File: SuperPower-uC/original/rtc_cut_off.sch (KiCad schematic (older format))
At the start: 6 parts, among them J4 Conn_01x02_Male, U3 RV-3028-C7

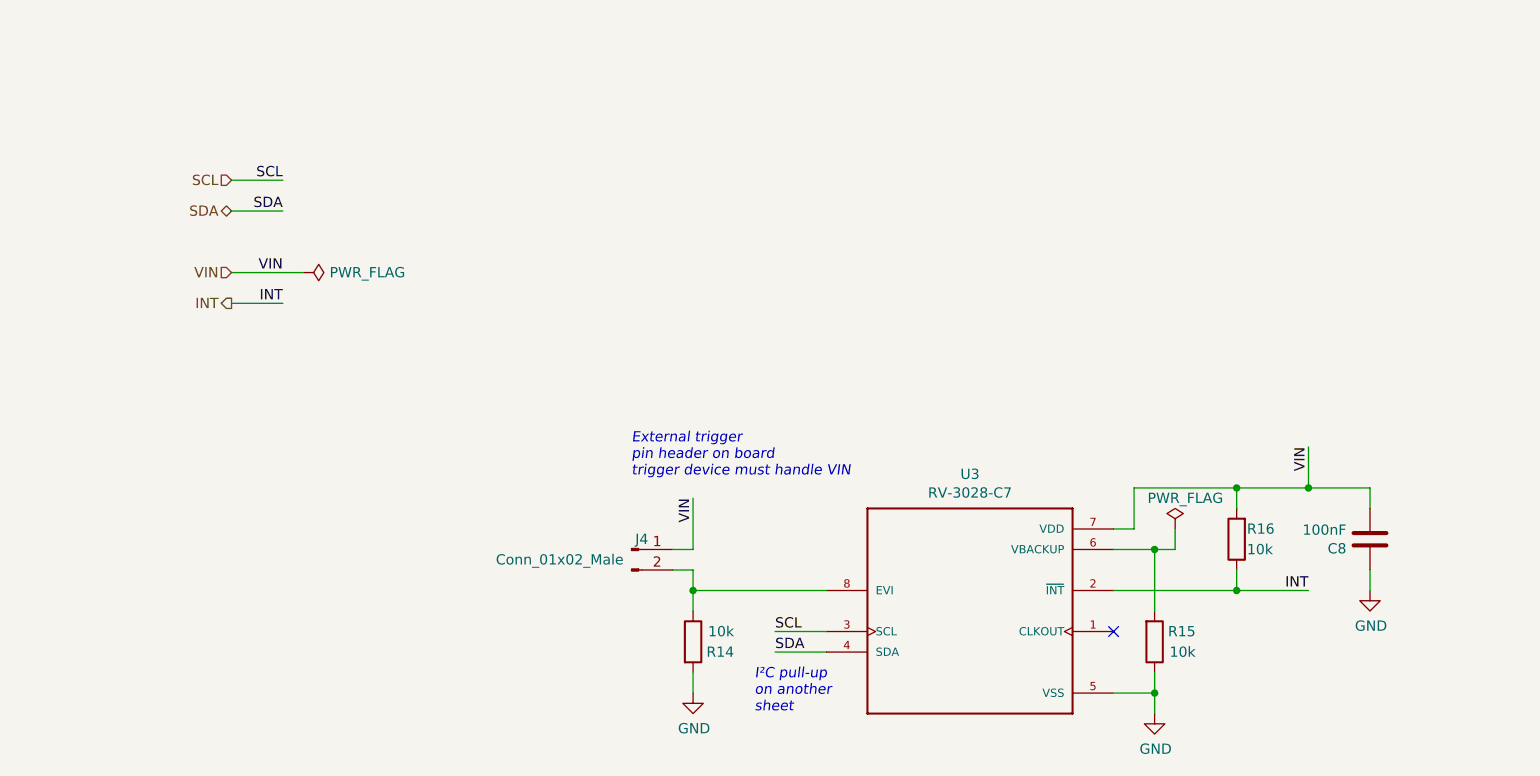
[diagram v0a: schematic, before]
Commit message: Complete rework of regulator design
Removed the old regulator in favor of the TPS63070 and TPS709.
Rewired the RTC and I2C pullups to the TPS709.
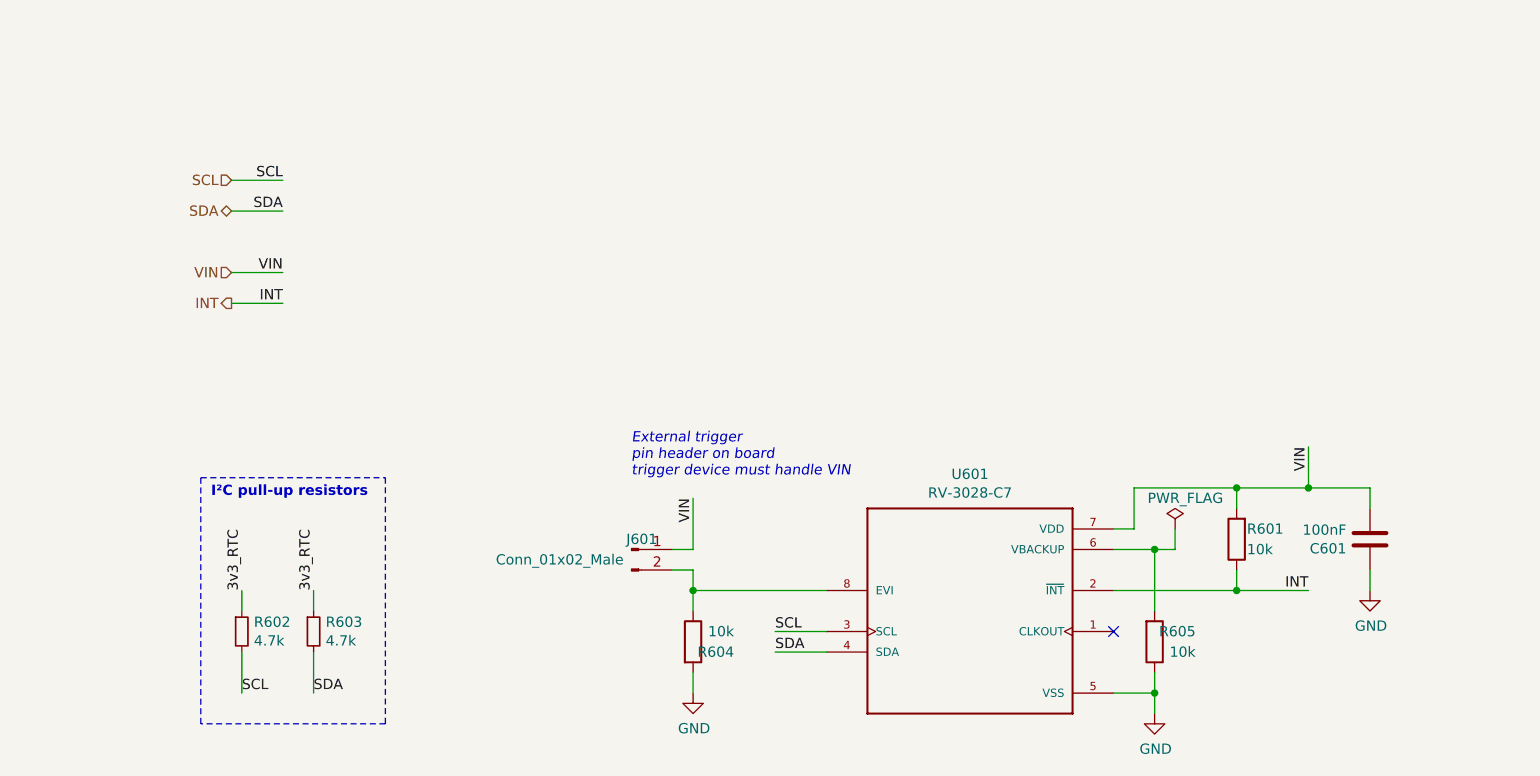
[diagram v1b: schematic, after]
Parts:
- added R602, R603: 4.7k, Resistor_SMD:R_0603_1608Metric_Pad0.98x0.95mm_HandSolder, symbol Device:R_Small
- renumbered C8 to C601, J4 to J601, R16 to R601, R14 to R604, R15 to R605, U3 to U601
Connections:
- net SCL: now also R602.2
- net SDA: now also R603.2
- new net 3v3_RTC: R602.1, R603.1
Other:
- note added: "I²C pull-up resistors"
- note removed: "I²C pull-up\non another\nsheet"
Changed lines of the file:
@@
 $Descr A4 11693 8268
 encoding utf-8
-Sheet 4 7
+Sheet 6 7
 Title "SuperPower-uC"
 Date "2020-09-20"
@@
 NoConn ~ 5900 3550
 $Comp
-L Device:R R15
+L Device:R R605
 U 1 1 5F716104
 P 6100 3600
-F 0 "R15" H 6300 3550 50  0000 R CNN
+F 0 "R605" H 6300 3550 50  0000 R CNN
 F 1 "10k" H 6300 3650 50  0000 R CNN
 F 2 "Resistor_SMD:R_0603_1608Metric_Pad1.05x0.95mm_HandSolder" V 6030 3600 50  0001 C CNN
@@
 $EndComp
 $Comp
-L power:GND #PWR025
+L power:GND #PWR0603
 U 1 1 5F71610D
 P 6100 3950
-F 0 "#PWR025" H 6100 3700 50  0001 C CNN
+F 0 "#PWR0603" H 6100 3700 50  0001 C CNN
 F 1 "GND" H 6105 3777 50  0000 C CNN
 F 2 "" H 6100 3950 50  0001 C CNN
@@
 $EndComp
 $Comp
-L Device:R R16
+L Device:R R601
 U 1 1 5F716136
 P 6500 3100
-F 0 "R16" H 6450 3050 50  0000 R CNN
+F 0 "R601" H 6450 3050 50  0000 R CNN
 F 1 "10k" H 6450 3150 50  0000 R CNN
 F 2 "Resistor_SMD:R_0603_1608Metric_Pad1.05x0.95mm_HandSolder" V 6430 3100 50  0001 C CNN
@@
 	4250 3650 4500 3650
 $Comp
-L RV-3028-C7:RV-3028-C7 U3
+L RV-3028-C7:RV-3028-C7 U601
 U 1 1 5F7160EF
 P 5200 3450
-F 0 "U3" H 5200 4117 50  0000 C CNN
+F 0 "U601" H 5200 4117 50  0000 C CNN
 F 1 "RV-3028-C7" H 5200 4026 50  0000 C CNN
 F 2 "RV-3028-C7:IC_RV-3028-C7" H 5200 3450 50  0001 L BNN
@@
 Text Label 1850 1950 2    50   ~ 0
 INT
-Text Notes 4150 3950 0    50   Italic 0
-I²C pull-up\non another\nsheet
 Text Notes 3550 2800 0    50   Italic 0
 External trigger\npin header on board\ntrigger device must handle VIN
@@
 Wire Wire Line
 	1600 1500 1850 1500
-$Comp
-L power:PWR_FLAG #FLG06
-U 1 1 5F765992
-P 1950 1800
-F 0 "#FLG06" H 1950 1875 50  0001 C CNN
-F 1 "PWR_FLAG" V 1950 1928 50  0000 L CNN
-F 2 "" H 1950 1800 50  0001 C CNN
-F 3 "~" H 1950 1800 50  0001 C CNN
-	1    1950 1800
-	0    1    1    0
-$EndComp
-Wire Wire Line
-	1600 1800 1950 1800
+Wire Wire Line
+	1600 1800 1850 1800
 Wire Wire Line
 	4500 3550 4250 3550
 $Comp
-L Device:C C8
+L Device:C C601
 U 1 1 5F716113
 P 7150 3100
-F 0 "C8" H 7265 3146 50  0000 L CNN
+F 0 "C601" H 7265 3146 50  0000 L CNN
 F 1 "100nF" H 7265 3055 50  0000 L CNN
 F 2 "Capacitor_SMD:C_0603_1608Metric_Pad1.05x0.95mm_HandSolder" H 7188 2950 50  0001 C CNN
@@
 INT
 $Comp
-L power:PWR_FLAG #FLG07
+L power:PWR_FLAG #FLG0601
 U 1 1 5FABB3BB
 P 6200 3050
-F 0 "#FLG07" H 6200 3125 50  0001 C CNN
+F 0 "#FLG0601" H 6200 3125 50  0001 C CNN
 F 1 "PWR_FLAG" H 6250 3200 50  0000 C CNN
 F 2 "" H 6200 3050 50  0001 C CNN
@@
 	3850 3750 3850 3850
 $Comp
-L Connector:Conn_01x02_Male J4
+L Connector:Conn_01x02_Male J601
 U 1 1 5F78D93A
 P 3550 3150
-F 0 "J4" H 3600 3200 50  0000 C CNN
+F 0 "J601" H 3600 3200 50  0000 C CNN
 F 1 "Conn_01x02_Male" H 3200 3100 50  0000 C CNN
 F 2 "" H 3550 3150 50  0001 C CNN
@@
 VIN
 $Comp
-L Device:R R14
+L Device:R R604
 U 1 1 5F716154
 P 3850 3600
-F 0 "R14" H 4050 3550 50  0000 R CNN
+F 0 "R604" H 4050 3550 50  0000 R CNN
 F 1 "10k" H 4050 3650 50  0000 R CNN
 F 2 "Resistor_SMD:R_0603_1608Metric_Pad1.05x0.95mm_HandSolder" V 3780 3600 50  0001 C CNN
@@
 $EndComp
 $Comp
-L power:GND #PWR024
+L power:GND #PWR0602
 U 1 1 5F716148
 P 3850 3850
-F 0 "#PWR024" H 3850 3600 50  0001 C CNN
+F 0 "#PWR0602" H 3850 3600 50  0001 C CNN
 F 1 "GND" H 3855 3677 50  0000 C CNN
 F 2 "" H 3850 3850 50  0001 C CNN
@@
 Connection ~ 6100 3150
 $Comp
-L power:GND #PWR026
+L power:GND #PWR0601
 U 1 1 5FBD2731
 P 7150 3350
-F 0 "#PWR026" H 7150 3100 50  0001 C CNN
+F 0 "#PWR0601" H 7150 3100 50  0001 C CNN
 F 1 "GND" H 7155 3177 50  0000 C CNN
 F 2 "" H 7150 3350 50  0001 C CNN
@@
 Wire Wire Line
 	6850 2650 6850 2850
+$Comp
+L Device:R_Small R?
+U 1 1 5FB76F56
+P 2000 3550
+AR Path="/5F63A193/5FB76F56" Ref="R?"  Part="1"
+AR Path="/5F63A00B/5FB76F56" Ref="R603"  Part="1"
+F 0 "R603" H 2059 3596 50  0000 L CNN
+F 1 "4.7k" H 2059 3505 50  0000 L CNN
+F 2 "Resistor_SMD:R_0603_1608Metric_Pad0.98x0.95mm_HandSolder" H 2000 3550 50  0001 C CNN
+F 3 "~" H 2000 3550 50  0001 C CNN
+	1    2000 3550
+	1    0    0    -1
+$EndComp
+$Comp
+L Device:R_Small R?
+U 1 1 5FB76F5C
+P 1650 3550
+AR Path="/5F63A193/5FB76F5C" Ref="R?"  Part="1"
+AR Path="/5F63A00B/5FB76F5C" Ref="R602"  Part="1"
+F 0 "R602" H 1709 3596 50  0000 L CNN
+F 1 "4.7k" H 1709 3505 50  0000 L CNN
+F 2 "Resistor_SMD:R_0603_1608Metric_Pad0.98x0.95mm_HandSolder" H 1650 3550 50  0001 C CNN
+F 3 "~" H 1650 3550 50  0001 C CNN
+	1    1650 3550
+	1    0    0    -1
+$EndComp
+Wire Wire Line
+	1650 3350 1650 3450
+Wire Wire Line
+	2000 3350 2000 3450
+Wire Wire Line
+	2000 3650 2000 3850
+Wire Wire Line
+	1650 3650 1650 3850
+Text Notes 1500 2900 0    50   ~ 10
+I²C pull-up resistors
+Wire Notes Line
+	1450 2800 2350 2800
+Wire Notes Line
+	1450 4000 1450 2800
+Wire Notes Line
+	2350 4000 1450 4000
+Wire Notes Line
+	2350 2800 2350 4000
+Text Label 1650 3350 1    50   ~ 0
+3v3_RTC
+Text Label 2000 3350 1    50   ~ 0
+3v3_RTC
+Text Label 2000 3850 0    50   ~ 0
+SDA
+Text Label 1650 3850 0    50   ~ 0
+SCL
 $EndSCHEMATC

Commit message: Changed 10k pulldowns to 100k. Cosmetics.
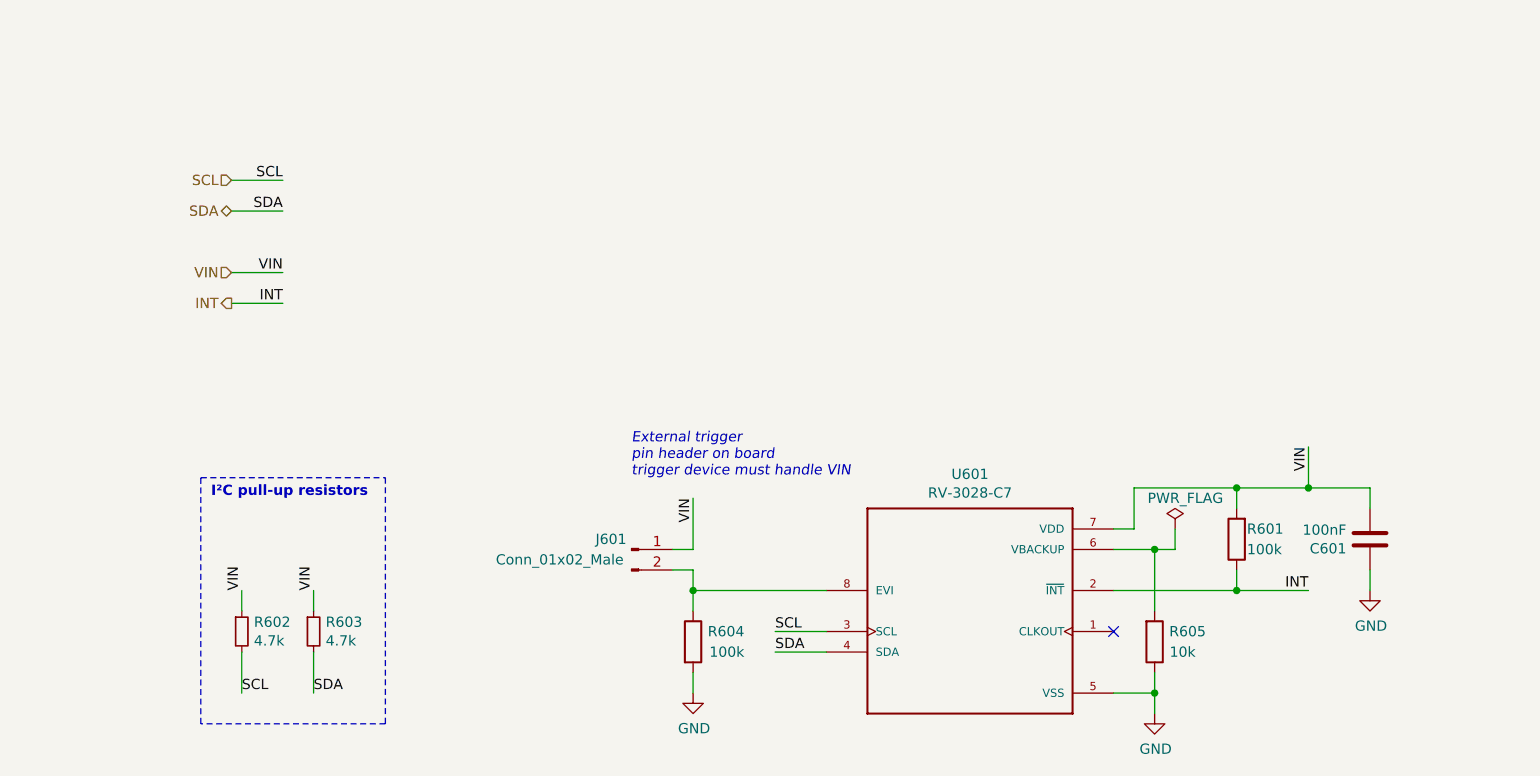
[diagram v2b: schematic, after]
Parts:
- R601, R604: value 10k -> 100k
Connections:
- net 3v3_RTC is gone; now on net VIN: R602.1, R603.1
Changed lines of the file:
@@
 U 1 1 5F716104
 P 6100 3600
-F 0 "R605" H 6300 3550 50  0000 R CNN
+F 0 "R605" H 6350 3550 50  0000 R CNN
 F 1 "10k" H 6300 3650 50  0000 R CNN
 F 2 "Resistor_SMD:R_0603_1608Metric_Pad1.05x0.95mm_HandSolder" V 6030 3600 50  0001 C CNN
@@
 P 6500 3100
 F 0 "R601" H 6450 3050 50  0000 R CNN
-F 1 "10k" H 6450 3150 50  0000 R CNN
+F 1 "100k" H 6450 3150 50  0000 R CNN
 F 2 "Resistor_SMD:R_0603_1608Metric_Pad1.05x0.95mm_HandSolder" V 6430 3100 50  0001 C CNN
 F 3 "~" H 6500 3100 50  0001 C CNN
@@
 U 1 1 5F78D93A
 P 3550 3150
-F 0 "J601" H 3600 3200 50  0000 C CNN
+F 0 "J601" H 3450 3200 50  0000 C CNN
 F 1 "Conn_01x02_Male" H 3200 3100 50  0000 C CNN
 F 2 "" H 3550 3150 50  0001 C CNN
@@
 U 1 1 5F716154
 P 3850 3600
-F 0 "R604" H 4050 3550 50  0000 R CNN
-F 1 "10k" H 4050 3650 50  0000 R CNN
+F 0 "R604" H 4100 3650 50  0000 R CNN
+F 1 "100k" H 4100 3550 50  0000 R CNN
 F 2 "Resistor_SMD:R_0603_1608Metric_Pad1.05x0.95mm_HandSolder" V 3780 3600 50  0001 C CNN
 F 3 "~" H 3850 3600 50  0001 C CNN
@@
 	2350 2800 2350 4000
 Text Label 1650 3350 1    50   ~ 0
-3v3_RTC
+VIN
 Text Label 2000 3350 1    50   ~ 0
-3v3_RTC
+VIN
 Text Label 2000 3850 0    50   ~ 0
 SDA

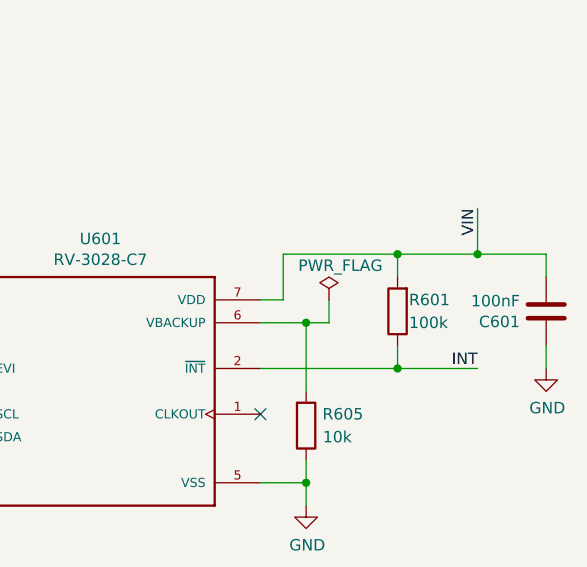
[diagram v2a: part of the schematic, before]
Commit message: Apply first batch of changes fro review ticket
https://github.com/Informaticore/SuperPower/issues/58
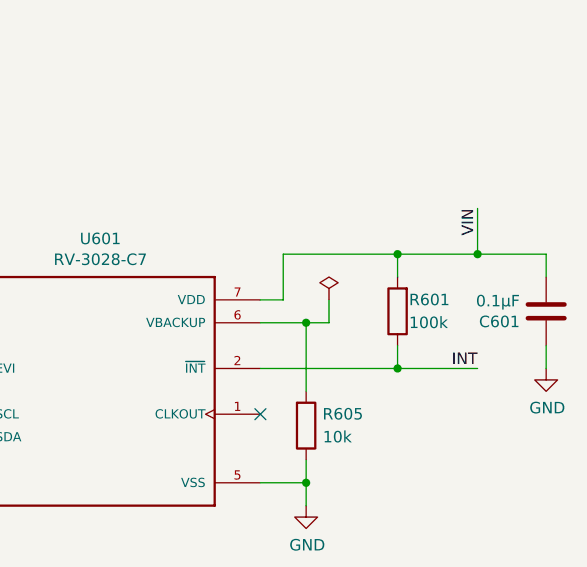
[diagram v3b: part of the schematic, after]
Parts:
- C601: value 100nF -> 0.1µF; footprint Capacitor_SMD:C_0603_1608Metric_Pad1.05x0.95mm_HandSolder -> Capacitors_SMD:C_0603
- R601, R604, R605: footprint Resistor_SMD:R_0603_1608Metric_Pad1.05x0.95mm_HandSolder -> Resistors_SMD:R_0603
- R602, R603: footprint Resistor_SMD:R_0603_1608Metric_Pad0.98x0.95mm_HandSolder -> Resistors_SMD:R_0603
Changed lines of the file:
@@
 F 0 "R605" H 6350 3550 50  0000 R CNN
 F 1 "10k" H 6300 3650 50  0000 R CNN
-F 2 "Resistor_SMD:R_0603_1608Metric_Pad1.05x0.95mm_HandSolder" V 6030 3600 50  0001 C CNN
+F 2 "Resistors_SMD:R_0603" V 6030 3600 50  0001 C CNN
 F 3 "~" H 6100 3600 50  0001 C CNN
 	1    6100 3600
@@
 F 0 "R601" H 6450 3050 50  0000 R CNN
 F 1 "100k" H 6450 3150 50  0000 R CNN
-F 2 "Resistor_SMD:R_0603_1608Metric_Pad1.05x0.95mm_HandSolder" V 6430 3100 50  0001 C CNN
+F 2 "Resistors_SMD:R_0603" V 6430 3100 50  0001 C CNN
 F 3 "~" H 6500 3100 50  0001 C CNN
 	1    6500 3100
@@
 P 7150 3100
 F 0 "C601" H 7265 3146 50  0000 L CNN
-F 1 "100nF" H 7265 3055 50  0000 L CNN
-F 2 "Capacitor_SMD:C_0603_1608Metric_Pad1.05x0.95mm_HandSolder" H 7188 2950 50  0001 C CNN
+F 1 "0.1µF" H 7265 3055 50  0000 L CNN
+F 2 "Capacitors_SMD:C_0603" H 7188 2950 50  0001 C CNN
 F 3 "~" H 7150 3100 50  0001 C CNN
 	1    7150 3100
@@
 P 6200 3050
 F 0 "#FLG0601" H 6200 3125 50  0001 C CNN
-F 1 "PWR_FLAG" H 6250 3200 50  0000 C CNN
+F 1 "PWR_FLAG" H 6250 3200 50  0001 C CNN
 F 2 "" H 6200 3050 50  0001 C CNN
 F 3 "~" H 6200 3050 50  0001 C CNN
@@
 F 0 "R604" H 4100 3650 50  0000 R CNN
 F 1 "100k" H 4100 3550 50  0000 R CNN
-F 2 "Resistor_SMD:R_0603_1608Metric_Pad1.05x0.95mm_HandSolder" V 3780 3600 50  0001 C CNN
+F 2 "Resistors_SMD:R_0603" V 3780 3600 50  0001 C CNN
 F 3 "~" H 3850 3600 50  0001 C CNN
 	1    3850 3600
@@
 F 0 "R603" H 2059 3596 50  0000 L CNN
 F 1 "4.7k" H 2059 3505 50  0000 L CNN
-F 2 "Resistor_SMD:R_0603_1608Metric_Pad0.98x0.95mm_HandSolder" H 2000 3550 50  0001 C CNN
+F 2 "Resistors_SMD:R_0603" H 2000 3550 50  0001 C CNN
 F 3 "~" H 2000 3550 50  0001 C CNN
 	1    2000 3550
@@
 F 0 "R602" H 1709 3596 50  0000 L CNN
 F 1 "4.7k" H 1709 3505 50  0000 L CNN
-F 2 "Resistor_SMD:R_0603_1608Metric_Pad0.98x0.95mm_HandSolder" H 1650 3550 50  0001 C CNN
+F 2 "Resistors_SMD:R_0603" H 1650 3550 50  0001 C CNN
 F 3 "~" H 1650 3550 50  0001 C CNN
 	1    1650 3550

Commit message: Applied more changes from review
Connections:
- net VIN renamed 3v3_RTC
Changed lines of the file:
@@
 Text HLabel 1600 1500 0    50   BiDi ~ 0
 SDA
-Text HLabel 1600 1800 0    50   Input ~ 0
-VIN
 Text HLabel 1600 1950 0    50   Output ~ 0
 INT
@@
 Text Label 1850 1500 2    50   ~ 0
 SDA
-Text Label 1850 1800 2    50   ~ 0
-VIN
 Text Label 1850 1950 2    50   ~ 0
 INT
-Text Notes 3550 2800 0    50   Italic 0
-External trigger\npin header on board\ntrigger device must handle VIN
 Wire Wire Line
 	1600 1950 1850 1950
@@
 Wire Wire Line
 	1600 1500 1850 1500
-Wire Wire Line
-	1600 1800 1850 1800
 Wire Wire Line
 	4500 3550 4250 3550
@@
 	1    0    0    -1
 $EndComp
-Wire Wire Line
-	3850 2900 3850 3150
-Text Label 3850 2900 3    50   ~ 0
-VIN
 $Comp
 L Device:R R604
@@
 Wire Wire Line
 	6500 3350 6850 3350
-Text Label 6850 2650 3    50   ~ 0
-VIN
 Wire Wire Line
 	6850 2850 7150 2850
@@
 	6500 2850 6850 2850
 Connection ~ 6850 2850
-Wire Wire Line
-	6850 2650 6850 2850
 $Comp
 L Device:R_Small R?
@@
 $EndComp
 Wire Wire Line
-	1650 3350 1650 3450
-Wire Wire Line
-	2000 3350 2000 3450
-Wire Wire Line
 	2000 3650 2000 3850
 Wire Wire Line
@@
 Wire Notes Line
 	2350 2800 2350 4000
-Text Label 1650 3350 1    50   ~ 0
-VIN
-Text Label 2000 3350 1    50   ~ 0
-VIN
 Text Label 2000 3850 0    50   ~ 0
 SDA
 Text Label 1650 3850 0    50   ~ 0
 SCL
+Text HLabel 1600 1800 0    50   Input ~ 0
+3v3_RTC
+Text Label 6850 2650 3    50   ~ 0
+VIN
+Wire Wire Line
+	6850 2650 6850 2850
+Wire Wire Line
+	3850 2900 3850 3150
+Text Label 3850 2900 3    50   ~ 0
+VIN
+Text Notes 3550 2800 0    50   Italic 0
+External trigger\npin header on board\ntrigger device must handle VIN
+Text Label 2000 3200 3    50   ~ 0
+VIN
+Text Label 1650 3200 3    50   ~ 0
+VIN
+Wire Wire Line
+	1600 1800 1850 1800
+Text Label 1850 1800 2    50   ~ 0
+VIN
+Wire Wire Line
+	2000 3200 2000 3450
+Wire Wire Line
+	1650 3200 1650 3450
 $EndSCHEMATC

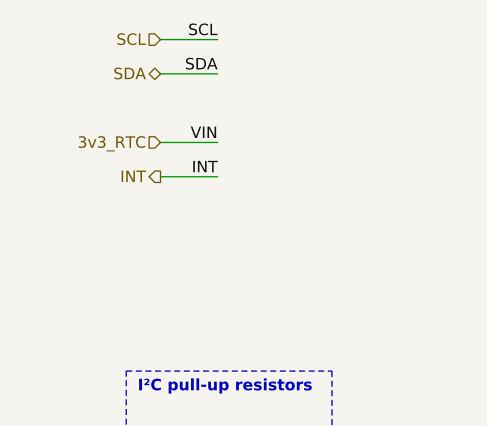
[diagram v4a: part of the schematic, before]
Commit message: Update Global Labels on main sheet and sub-sheets
3V3_RTC updates
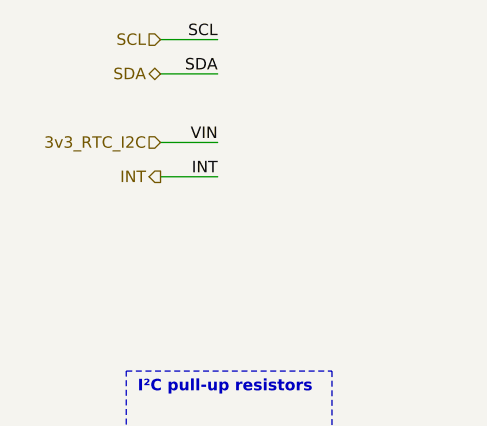
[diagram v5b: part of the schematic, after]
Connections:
- net 3v3_RTC renamed 3v3_RTC_I2C
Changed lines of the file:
@@
 SCL
 Text HLabel 1600 1800 0    50   Input ~ 0
-3v3_RTC
+3v3_RTC_I2C
 Text Label 6850 2650 3    50   ~ 0
 VIN
